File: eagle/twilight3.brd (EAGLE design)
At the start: 59 x 23 mm, 19 parts, among them IC1 TINY85, IC2 7805TV, Q1 IRF540

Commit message: changing resistor sizes and orientations; move ldr to edge of board
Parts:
- R1, R2, R4, R5: device resistor:0204/7 -> resistor:0207/2V
- R3, R6: device resistor:0204/7 -> resistor:0207/10
- moved R6 12.1 mm to (50.0, 76.0), turned to 90 degrees
- moved R1 7.15 mm to (43.0, 76.0), turned to 180 degrees
- moved R7 6.08 mm to (42.0, 67.0)
- moved R2 5.20 mm to (43.0, 72.0)
- moved R3 4.52 mm to (47.0, 76.0), turned to 90 degrees
- moved C3 1.00 mm to (23.1, 76.2)
- moved IC1 1.00 mm to (32.0, 69.8)
- moved R4 0.94 mm to (22.0, 72.0), turned to 180 degrees
- moved R5 0.53 mm to (16.0, 72.0), turned to 270 degrees
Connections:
- net GND: now also R1.1, R6.1; no longer R1.2, R6.2
- net N$2: now also R5.2; no longer R5.1
- net N$3: now also R4.1; no longer R4.2
- net N$5: now also R3.1; no longer R3.2
- net N$6: now also R3.2, R6.2; no longer R3.1, R6.1
- net N$9: now also R1.2; no longer R1.1
- net VCC: now also R4.2, R5.1; no longer R4.1, R5.2
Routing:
- net GND: track 91.5 -> 0.00 mm
- net N$6: track 20.0 -> 7.66 mm
- net VCC: track 44.1 -> 55.6 mm
- net N$4: track 14.5 -> 11.9 mm
- net N$9: track 14.9 -> 17.4 mm
- net N$2: track 24.9 -> 27.2 mm
- net GNDOUT: track 13.3 -> 11.1 mm
- net N$3: track 6.64 -> 8.82 mm
- net N$5: track 13.3 -> 15.2 mm
- net +12V: track 60.6 -> 59.0 mm
- net N$1: track 11.0 -> 12.2 mm
- added copper zone on layer 16, net GND

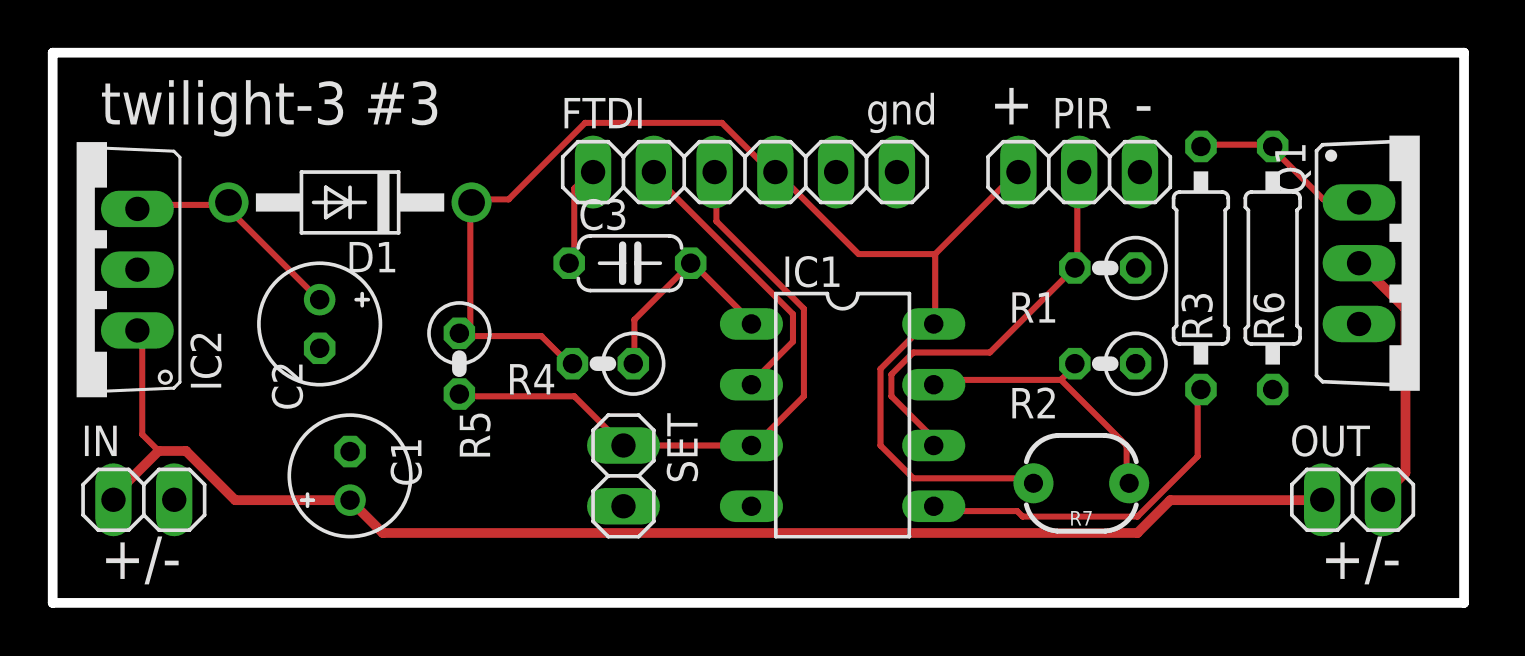
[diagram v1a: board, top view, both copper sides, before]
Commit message: adding bypass capacitor
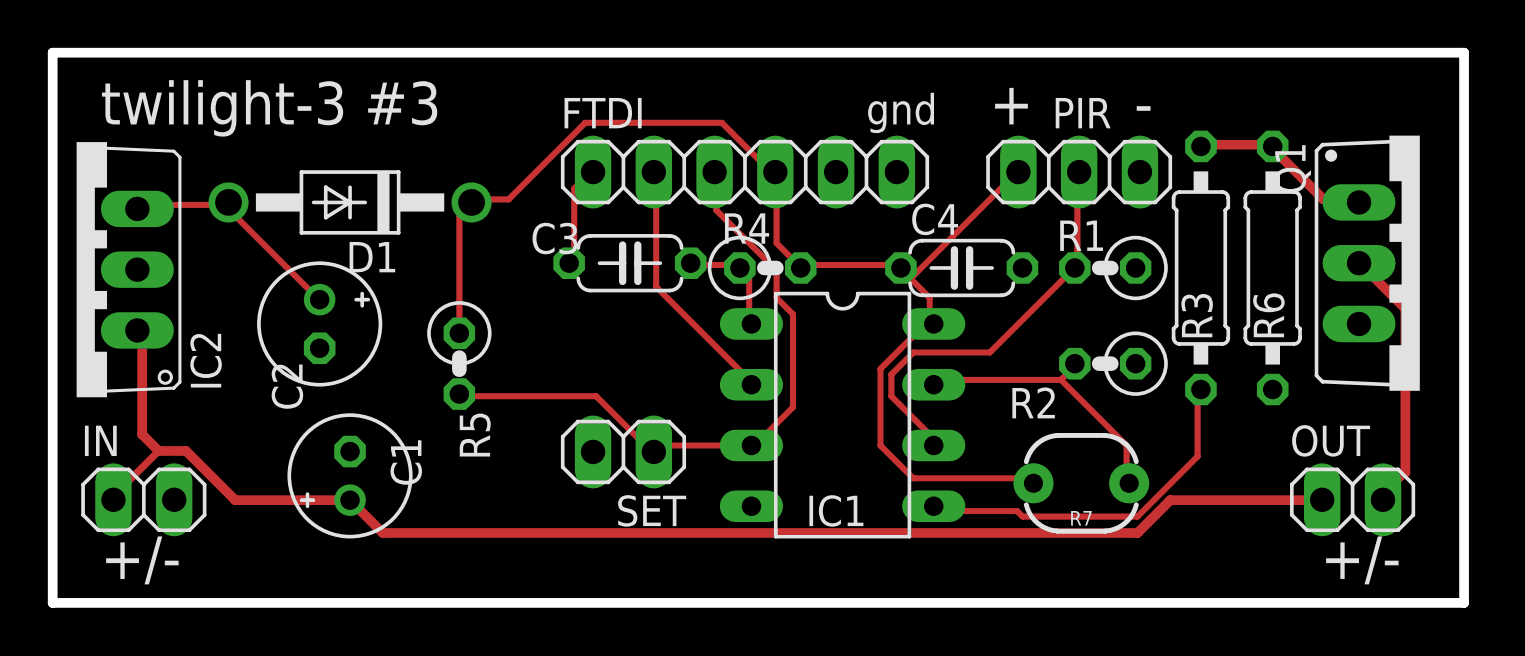
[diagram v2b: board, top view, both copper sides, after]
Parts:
- added C4: 100n, resistor:C050-024X044
- moved R4 8.06 mm to (29.0, 76.0), turned to 0 degrees
- moved SET 1.00 mm to (22.9, 68.3), turned to 180 degrees
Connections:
- net GND: now also C4.2
- net VCC: now also C4.1
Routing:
- net N$3: track 8.82 -> 4.69 mm
- net VCC: track 55.6 -> 52.3 mm
- net N$1: track 12.2 -> 10.6 mm

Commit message: add reset header
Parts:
- added RST: (no value), pinhead:1X02
- moved R5 1.00 mm to (16.0, 71.0)
- moved SET 1.00 mm to (22.9, 67.3)
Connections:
- net GND: now also RST.2
- net N$3: now also RST.1
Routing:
- net N$1: track 10.6 -> 15.6 mm
- net N$3: track 4.69 -> 9.31 mm
- net VCC: track 52.3 -> 53.3 mm
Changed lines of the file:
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@@
 <attribute name="VALUE" x="38.1" y="76.835" size="1.27" layer="27"/>
 </element>
-<element name="SET" library="pinhead" package="1X02" value="" x="22.86" y="68.31" rot="R180"/>
+<element name="SET" library="pinhead" package="1X02" value="" x="22.86" y="67.31" smashed="yes" rot="R180">
+<attribute name="NAME" x="20.4762" y="67.4812" size="1.27" layer="25" ratio="10" rot="R180"/>
+<attribute name="VALUE" x="25.4" y="70.485" size="1.27" layer="27" rot="R180"/>
+</element>
 <element name="C1" library="rcl" package="E2-5" value="10uF" x="11.43" y="67.31" smashed="yes" rot="R90">
 <attribute name="NAME" x="14.414" y="66.85" size="1.27" layer="25" ratio="10" rot="R90"/>
@@
 <element name="FTDI" library="pinhead" package="1X06" value="" x="27.94" y="80.01"/>
 <element name="C3" library="resistor" package="C050-024X044" value="100n" x="23.13" y="76.2" smashed="yes">
-<attribute name="NAME" x="18.971" y="76.597" size="1.27" layer="25" ratio="10"/>
+<attribute name="NAME" x="18.971" y="74.597" size="1.27" layer="25" ratio="10"/>
 <attribute name="VALUE" x="22.971" y="73.533" size="1.27" layer="27" ratio="10"/>
 </element>
@@
 <attribute name="VALUE" x="29.9492" y="76.7648" size="1.27" layer="27" ratio="10"/>
 </element>
-<element name="R5" library="resistor" package="0207/2V" value="10k" x="16" y="72" smashed="yes" rot="R270">
-<attribute name="NAME" x="16.016" y="70.0508" size="1.27" layer="25" ratio="10" rot="R270"/>
-<attribute name="VALUE" x="16.7648" y="77.0508" size="1.27" layer="27" ratio="10" rot="R270"/>
+<element name="R5" library="resistor" package="0207/2V" value="10k" x="16" y="71" smashed="yes" rot="R270">
+<attribute name="NAME" x="16.016" y="69.0508" size="1.27" layer="25" ratio="10" rot="R270"/>
+<attribute name="VALUE" x="16.7648" y="76.0508" size="1.27" layer="27" ratio="10" rot="R270"/>
 </element>
 <element name="R1" library="resistor" package="0207/2V" value="22k" x="43" y="76" smashed="yes" rot="R180">
@@
 <attribute name="NAME" x="34.841" y="77.397" size="1.27" layer="25" ratio="10"/>
 <attribute name="VALUE" x="37.841" y="73.333" size="1.27" layer="27" ratio="10"/>
+</element>
+<element name="RST" library="pinhead" package="1X02" value="" x="23" y="72" smashed="yes" rot="R180">
+<attribute name="NAME" x="20.6162" y="72.1712" size="1.27" layer="25" ratio="10" rot="R180"/>
+<attribute name="VALUE" x="25.54" y="75.175" size="1.27" layer="27" rot="R180"/>
 </element>
 </elements>
@@
 <contactref element="R5" pad="1"/>
 <contactref element="C4" pad="1"/>
-<wire x1="16.002" y1="78.1812" x2="16.002" y2="73.3806" width="0.254" layer="1"/>
+<wire x1="16.002" y1="78.1812" x2="16.002" y2="72.4662" width="0.254" layer="1"/>
 <wire x1="16.4592" y1="78.6384" x2="16.002" y2="78.1812" width="0.254" layer="1"/>
-<wire x1="16.002" y1="73.3806" x2="16" y2="73.27" width="0.254" layer="1"/>
+<wire x1="16.002" y1="72.4662" x2="16" y2="72.27" width="0.254" layer="1"/>
 <wire x1="16.4592" y1="78.6384" x2="16.51" y2="78.74" width="0.254" layer="1"/>
 <wire x1="34.29" y1="76.1238" x2="30.4038" y2="76.1238" width="0.254" layer="1"/>
@@
 <contactref element="IC2" pad="2"/>
 <contactref element="FTDI" pad="6"/>
-<contactref element="SET" pad="2"/>
 <contactref element="Q1" pad="S"/>
 <contactref element="PIR" pad="3"/>
@@
 <contactref element="R6" pad="1"/>
 <contactref element="C4" pad="2"/>
+<contactref element="RST" pad="2"/>
+<contactref element="SET" pad="2"/>
 </signal>
 <signal name="+12V">
@@
 <wire x1="4.572" y1="68.3514" x2="6.6294" y2="66.294" width="0.4064" layer="1"/>
 <wire x1="3.429" y1="68.3514" x2="4.572" y2="68.3514" width="0.4064" layer="1"/>
-<wire x1="1.6002" y1="66.5226" x2="3.429" y2="68.3514" width="0.3048" layer="1"/>
+<wire x1="1.6002" y1="66.5226" x2="3.429" y2="68.3514" width="0.4064" layer="1"/>
 <wire x1="1.6002" y1="66.5226" x2="1.54" y2="66.31" width="0.254" layer="1"/>
 <wire x1="2.7432" y1="69.0372" x2="2.7432" y2="73.3806" width="0.4064" layer="1"/>
 <wire x1="3.429" y1="68.3514" x2="2.7432" y2="69.0372" width="0.4064" layer="1"/>
 <wire x1="2.7432" y1="73.3806" x2="2.54" y2="73.39" width="0.254" layer="1"/>
-<wire x1="45.72" y1="66.294" x2="51.8922" y2="66.294" width="0.4064" layer="1"/>
-<wire x1="44.3484" y1="64.9224" x2="45.72" y2="66.294" width="0.4064" layer="1"/>
-<wire x1="12.8016" y1="64.9224" x2="44.3484" y2="64.9224" width="0.4064" layer="1"/>
+<wire x1="48.72" y1="66.294" x2="51.8922" y2="66.294" width="0.4064" layer="1"/>
+<wire x1="47.3484" y1="64.9224" x2="48.72" y2="66.294" width="0.4064" layer="1"/>
+<wire x1="12.8016" y1="64.9224" x2="47.3484" y2="64.9224" width="0.4064" layer="1"/>
 <wire x1="11.43" y1="66.294" x2="12.8016" y2="64.9224" width="0.4064" layer="1"/>
 <wire x1="51.8922" y1="66.294" x2="52.07" y2="66.31" width="0.254" layer="1"/>
@@
 <wire x1="55.5498" y1="74.295" x2="53.721" y2="76.1238" width="0.4064" layer="1"/>
 <wire x1="55.5498" y1="67.437" x2="55.5498" y2="74.295" width="0.4064" layer="1"/>
-<wire x1="54.6354" y1="66.5226" x2="55.5498" y2="67.437" width="0.3048" layer="1"/>
+<wire x1="54.6354" y1="66.5226" x2="55.5498" y2="67.437" width="0.4064" layer="1"/>
 <wire x1="53.721" y1="76.1238" x2="53.61" y2="76.2" width="0.254" layer="1"/>
 <wire x1="54.6354" y1="66.5226" x2="54.61" y2="66.31" width="0.254" layer="1"/>
@@
 <contactref element="IC1" pad="2"/>
 <contactref element="FTDI" pad="2"/>
-<wire x1="24.2316" y1="75.2094" x2="28.1178" y2="71.3232" width="0.254" layer="1"/>
-<wire x1="24.2316" y1="80.01" x2="24.2316" y2="75.2094" width="0.254" layer="1"/>
-<wire x1="28.1178" y1="71.3232" x2="28.21" y2="71.12" width="0.254" layer="1"/>
-<wire x1="24.2316" y1="80.01" x2="24.13" y2="80.01" width="0.254" layer="1"/>
+<wire x1="25.8318" y1="71.0946" x2="28.1178" y2="71.0946" width="0.254" layer="1"/>
+<wire x1="24.6888" y1="69.9516" x2="25.8318" y2="71.0946" width="0.254" layer="1"/>
+<wire x1="24.003" y1="69.9516" x2="24.6888" y2="69.9516" width="0.254" layer="1"/>
+<wire x1="23.0886" y1="70.866" x2="24.003" y2="69.9516" width="0.254" layer="1"/>
+<wire x1="23.0886" y1="79.0956" x2="23.0886" y2="70.866" width="0.254" layer="1"/>
+<wire x1="24.003" y1="80.01" x2="23.0886" y2="79.0956" width="0.254" layer="1"/>
+<wire x1="28.1178" y1="71.0946" x2="28.21" y2="71.12" width="0.254" layer="1"/>
+<wire x1="24.003" y1="80.01" x2="24.13" y2="80.01" width="0.254" layer="1"/>
 </signal>
 <signal name="N$7">
@@
 <contactref element="IC1" pad="1"/>
 <contactref element="R4" pad="1"/>
+<contactref element="RST" pad="1"/>
+<wire x1="25.8318" y1="76.1238" x2="27.6606" y2="76.1238" width="0.254" layer="1"/>
+<wire x1="27.6606" y1="76.1238" x2="27.73" y2="76" width="0.254" layer="1"/>
+<wire x1="25.8318" y1="76.1238" x2="25.67" y2="76.2" width="0.254" layer="1"/>
 <wire x1="28.1178" y1="75.6666" x2="28.1178" y2="73.8378" width="0.254" layer="1"/>
 <wire x1="27.8892" y1="75.8952" x2="28.1178" y2="75.6666" width="0.254" layer="1"/>
 <wire x1="28.1178" y1="73.8378" x2="28.21" y2="73.66" width="0.254" layer="1"/>
 <wire x1="27.8892" y1="75.8952" x2="27.73" y2="76" width="0.254" layer="1"/>
-<wire x1="27.6606" y1="76.1238" x2="25.8318" y2="76.1238" width="0.254" layer="1"/>
-<wire x1="25.8318" y1="76.1238" x2="25.67" y2="76.2" width="0.254" layer="1"/>
-<wire x1="27.6606" y1="76.1238" x2="27.73" y2="76" width="0.254" layer="1"/>
+<wire x1="26.5176" y1="72.009" x2="24.4602" y2="72.009" width="0.254" layer="1"/>
+<wire x1="28.1178" y1="73.6092" x2="26.5176" y2="72.009" width="0.254" layer="1"/>
+<wire x1="24.4602" y1="72.009" x2="24.27" y2="72" width="0.254" layer="1"/>
+<wire x1="28.1178" y1="73.6092" x2="28.21" y2="73.66" width="0.254" layer="1"/>
 </signal>
 <signal name="N$2">
@@
 <contactref element="SET" pad="1"/>
 <contactref element="R5" pad="2"/>
-<wire x1="24.4602" y1="68.58" x2="28.21" y2="68.58" width="0.254" layer="1"/>
-<wire x1="24.2316" y1="68.3514" x2="24.4602" y2="68.58" width="0.254" layer="1"/>
-<wire x1="24.2316" y1="68.3514" x2="24.13" y2="68.31" width="0.254" layer="1"/>
-<wire x1="21.717" y1="70.6374" x2="16.002" y2="70.6374" width="0.254" layer="1"/>
-<wire x1="24.003" y1="68.3514" x2="21.717" y2="70.6374" width="0.254" layer="1"/>
-<wire x1="16.002" y1="70.6374" x2="16" y2="70.73" width="0.254" layer="1"/>
-<wire x1="24.003" y1="68.3514" x2="24.13" y2="68.31" width="0.254" layer="1"/>
+<wire x1="25.3746" y1="68.58" x2="28.21" y2="68.58" width="0.254" layer="1"/>
+<wire x1="24.2316" y1="67.437" x2="25.3746" y2="68.58" width="0.254" layer="1"/>
+<wire x1="24.2316" y1="67.437" x2="24.13" y2="67.31" width="0.254" layer="1"/>
+<wire x1="21.717" y1="69.723" x2="16.002" y2="69.723" width="0.254" layer="1"/>
+<wire x1="24.13" y1="67.31" x2="21.717" y2="69.723" width="0.254" layer="1"/>
+<wire x1="16.002" y1="69.723" x2="16" y2="69.73" width="0.254" layer="1"/>
 <wire x1="26.7462" y1="78.4098" x2="26.7462" y2="80.01" width="0.254" layer="1"/>
 <wire x1="29.2608" y1="75.8952" x2="26.7462" y2="78.4098" width="0.254" layer="1"/>
@@
 <contactref element="R3" pad="2"/>
 <contactref element="R6" pad="2"/>
-<wire x1="49.8348" y1="81.153" x2="47.0916" y2="81.153" width="0.4064" layer="1"/>
+<wire x1="49.8348" y1="81.153" x2="47.0916" y2="81.153" width="0.254" layer="1"/>
 <wire x1="47.0916" y1="81.153" x2="47" y2="81.08" width="0.254" layer="1"/>
 <wire x1="49.8348" y1="81.153" x2="50" y2="81.08" width="0.254" layer="1"/>
-<wire x1="52.1208" y1="78.867" x2="53.4924" y2="78.867" width="0.4064" layer="1"/>
-<wire x1="50.0634" y1="80.9244" x2="52.1208" y2="78.867" width="0.4064" layer="1"/>
-<wire x1="53.4924" y1="78.867" x2="53.61" y2="78.74" width="0.4064" layer="1"/>
+<wire x1="52.1208" y1="78.867" x2="53.4924" y2="78.867" width="0.254" layer="1"/>
+<wire x1="50.0634" y1="80.9244" x2="52.1208" y2="78.867" width="0.254" layer="1"/>
+<wire x1="53.4924" y1="78.867" x2="53.61" y2="78.74" width="0.254" layer="1"/>
 <wire x1="50.0634" y1="80.9244" x2="50" y2="81.08" width="0.254" layer="1"/>
 </signal>
